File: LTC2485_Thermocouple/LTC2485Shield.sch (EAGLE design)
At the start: 13 parts

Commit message: Added OLED Shield Added LiPo Battery Charger Shield Updated outlines of all shields to match the cutout of the nodemcu board
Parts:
- removed JP1, JP2: (no value), SparkFun:M03LOCK
- added SJ1, SJ2: (no value), SparkFun:SOLDERJUMPER_2WAYT
- D2, D3: device SparkFun:DIODESMB -> SparkFun:DIODESOD
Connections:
- net GND: now also SJ1.1, SJ2.1, U$1.GND$10, U$1.GND$17, U$1.GND$24; no longer JP1.1, JP2.1
- net N$2: now also U$1.D7/GPIO13/RXD2/HSPID/SDA; no longer U$1.D7/GPIO13/RXD2/HSPID
- net N$6: now also SJ1.3, SJ2.3; no longer JP1.3, JP2.3
- net N$7: now also SJ1.2; no longer JP1.2
- net N$8: now also U$1.D6/GPIO12/HSPIQ/SCL; no longer U$1.D6/GPIO12/HSPIQ
- net N$9: now also SJ2.2; no longer JP2.2
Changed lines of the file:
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@@
 <?xml version="1.0" encoding="utf-8"?>
 <!DOCTYPE eagle SYSTEM "eagle.dtd">
-<eagle version="7.3.0">
+<eagle version="7.4.0">
 <drawing>
 <settings>
@@
 <part name="X1" library="con-wago-500" deviceset="W237-102" device=""/>
 <part name="R3" library="SparkFun" deviceset="RESISTOR" device="0402-RES" value="2k"/>
-<part name="D2" library="SparkFun" deviceset="DIODE" device="SMB"/>
-<part name="D3" library="SparkFun" deviceset="DIODE" device="SMB"/>
+<part name="D2" library="SparkFun" deviceset="DIODE" device="SOD"/>
+<part name="D3" library="SparkFun" deviceset="DIODE" device="SOD"/>
 <part name="R4" library="SparkFun" deviceset="RESISTOR" device="0402-RES" value="4.7k"/>
 <part name="P+2" library="SparkFun" deviceset="3.3V" device=""/>
 <part name="GND5" library="SparkFun" deviceset="GND" device=""/>
-<part name="JP1" library="SparkFun" deviceset="M03" device="LOCK"/>
-<part name="JP2" library="SparkFun" deviceset="M03" device="LOCK"/>
 <part name="P+4" library="SparkFun" deviceset="3.3V" device=""/>
+<part name="GND6" library="SparkFun" deviceset="GND" device=""/>
+<part name="SJ1" library="SparkFun" deviceset="SOLDERJUMPER_2WAY" device="T"/>
+<part name="SJ2" library="SparkFun" deviceset="SOLDERJUMPER_2WAY" device="T"/>
 </parts>
 <sheets>
@@
 <instance part="R4" gate="G$1" x="83.82" y="2.54" rot="R90"/>
 <instance part="P+2" gate="G$1" x="83.82" y="10.16"/>
-<instance part="GND5" gate="1" x="127" y="-12.7"/>
-<instance part="JP1" gate="G$1" x="91.44" y="-15.24" rot="R90"/>
-<instance part="JP2" gate="G$1" x="109.22" y="-15.24" rot="R90"/>
+<instance part="GND5" gate="1" x="127" y="-27.94"/>
 <instance part="P+4" gate="G$1" x="167.64" y="50.8"/>
+<instance part="GND6" gate="1" x="73.66" y="20.32"/>
+<instance part="SJ1" gate="G$1" x="91.44" y="-12.7" rot="R270"/>
+<instance part="SJ2" gate="G$1" x="109.22" y="-12.7" rot="R270"/>
 </instances>
 <busses>
@@
 <wire x1="7.62" y1="33.02" x2="-5.08" y2="33.02" width="0.1524" layer="91"/>
 <wire x1="-5.08" y1="33.02" x2="-5.08" y2="20.32" width="0.1524" layer="91"/>
+<pinref part="U$1" gate="G$1" pin="GND$10"/>
+<wire x1="7.62" y1="43.18" x2="-5.08" y2="43.18" width="0.1524" layer="91"/>
+<wire x1="-5.08" y1="43.18" x2="-5.08" y2="33.02" width="0.1524" layer="91"/>
+<junction x="-5.08" y="33.02"/>
 </segment>
 <segment>
@@
 </segment>
 <segment>
-<pinref part="JP1" gate="G$1" pin="1"/>
-<wire x1="93.98" y1="-7.62" x2="93.98" y2="-2.54" width="0.1524" layer="91"/>
 <pinref part="GND5" gate="1" pin="GND"/>
-<wire x1="93.98" y1="-2.54" x2="111.76" y2="-2.54" width="0.1524" layer="91"/>
-<wire x1="111.76" y1="-2.54" x2="127" y2="-2.54" width="0.1524" layer="91"/>
-<wire x1="127" y1="-2.54" x2="127" y2="-10.16" width="0.1524" layer="91"/>
-<pinref part="JP2" gate="G$1" pin="1"/>
-<wire x1="111.76" y1="-7.62" x2="111.76" y2="-2.54" width="0.1524" layer="91"/>
-<junction x="111.76" y="-2.54"/>
+<wire x1="99.06" y1="-20.32" x2="116.84" y2="-20.32" width="0.1524" layer="91"/>
+<wire x1="116.84" y1="-20.32" x2="127" y2="-20.32" width="0.1524" layer="91"/>
+<wire x1="127" y1="-20.32" x2="127" y2="-25.4" width="0.1524" layer="91"/>
+<junction x="116.84" y="-20.32"/>
+<pinref part="SJ1" gate="G$1" pin="1"/>
+<wire x1="96.52" y1="-12.7" x2="99.06" y2="-12.7" width="0.1524" layer="91"/>
+<wire x1="99.06" y1="-12.7" x2="99.06" y2="-20.32" width="0.1524" layer="91"/>
+<pinref part="SJ2" gate="G$1" pin="1"/>
+<wire x1="114.3" y1="-12.7" x2="116.84" y2="-12.7" width="0.1524" layer="91"/>
+<wire x1="116.84" y1="-12.7" x2="116.84" y2="-20.32" width="0.1524" layer="91"/>
+</segment>
+<segment>
+<pinref part="U$1" gate="G$1" pin="GND$17"/>
+<pinref part="GND6" gate="1" pin="GND"/>
+<wire x1="71.12" y1="33.02" x2="73.66" y2="33.02" width="0.1524" layer="91"/>
+<wire x1="73.66" y1="33.02" x2="73.66" y2="22.86" width="0.1524" layer="91"/>
+<pinref part="U$1" gate="G$1" pin="GND$24"/>
+<wire x1="71.12" y1="50.8" x2="73.66" y2="50.8" width="0.1524" layer="91"/>
+<wire x1="73.66" y1="50.8" x2="73.66" y2="33.02" width="0.1524" layer="91"/>
+<junction x="73.66" y="33.02"/>
 </segment>
 </net>
@@
 <net name="N$2" class="0">
 <segment>
-<pinref part="U$1" gate="G$1" pin="D7/GPIO13/RXD2/HSPID"/>
+<pinref part="U$1" gate="G$1" pin="D7/GPIO13/RXD2/HSPID/SDA"/>
 <wire x1="121.92" y1="43.18" x2="104.14" y2="43.18" width="0.1524" layer="91"/>
 <pinref part="U$2" gate="G$2" pin="SDA"/>
@@
 <net name="N$8" class="0">
 <segment>
-<pinref part="U$1" gate="G$1" pin="D6/GPIO12/HSPIQ"/>
+<pinref part="U$1" gate="G$1" pin="D6/GPIO12/HSPIQ/SCL"/>
 <pinref part="U$2" gate="G$2" pin="SCL"/>
 <wire x1="121.92" y1="45.72" x2="96.52" y2="45.72" width="0.1524" layer="91"/>
@@
 <pinref part="R4" gate="G$1" pin="1"/>
 <wire x1="83.82" y1="-2.54" x2="83.82" y2="-5.08" width="0.1524" layer="91"/>
-<pinref part="JP2" gate="G$1" pin="3"/>
-<wire x1="83.82" y1="-5.08" x2="88.9" y2="-5.08" width="0.1524" layer="91"/>
-<wire x1="88.9" y1="-5.08" x2="106.68" y2="-5.08" width="0.1524" layer="91"/>
-<wire x1="106.68" y1="-5.08" x2="106.68" y2="-7.62" width="0.1524" layer="91"/>
-<pinref part="JP1" gate="G$1" pin="3"/>
-<wire x1="88.9" y1="-5.08" x2="88.9" y2="-7.62" width="0.1524" layer="91"/>
-<junction x="88.9" y="-5.08"/>
+<wire x1="83.82" y1="-5.08" x2="101.6" y2="-5.08" width="0.1524" layer="91"/>
+<wire x1="101.6" y1="-5.08" x2="101.6" y2="-12.7" width="0.1524" layer="91"/>
+<junction x="83.82" y="-5.08"/>
+<pinref part="SJ1" gate="G$1" pin="3"/>
+<wire x1="86.36" y1="-12.7" x2="83.82" y2="-12.7" width="0.1524" layer="91"/>
+<wire x1="83.82" y1="-12.7" x2="83.82" y2="-5.08" width="0.1524" layer="91"/>
+<pinref part="SJ2" gate="G$1" pin="3"/>
+<wire x1="104.14" y1="-12.7" x2="101.6" y2="-12.7" width="0.1524" layer="91"/>
 </segment>
 </net>
@@
 <segment>
 <pinref part="U$2" gate="G$2" pin="A1"/>
-<pinref part="JP1" gate="G$1" pin="2"/>
 <wire x1="121.92" y1="38.1" x2="91.44" y2="38.1" width="0.1524" layer="91"/>
 <wire x1="91.44" y1="38.1" x2="91.44" y2="-7.62" width="0.1524" layer="91"/>
+<pinref part="SJ1" gate="G$1" pin="2"/>
 </segment>
 </net>
@@
 <segment>
 <pinref part="U$2" gate="G$2" pin="A0"/>
-<pinref part="JP2" gate="G$1" pin="2"/>
 <wire x1="121.92" y1="35.56" x2="109.22" y2="35.56" width="0.1524" layer="91"/>
 <wire x1="109.22" y1="35.56" x2="109.22" y2="-7.62" width="0.1524" layer="91"/>
-</segment>
-</net>
+<pinref part="SJ2" gate="G$1" pin="2"/>
+</segment>
+</net>

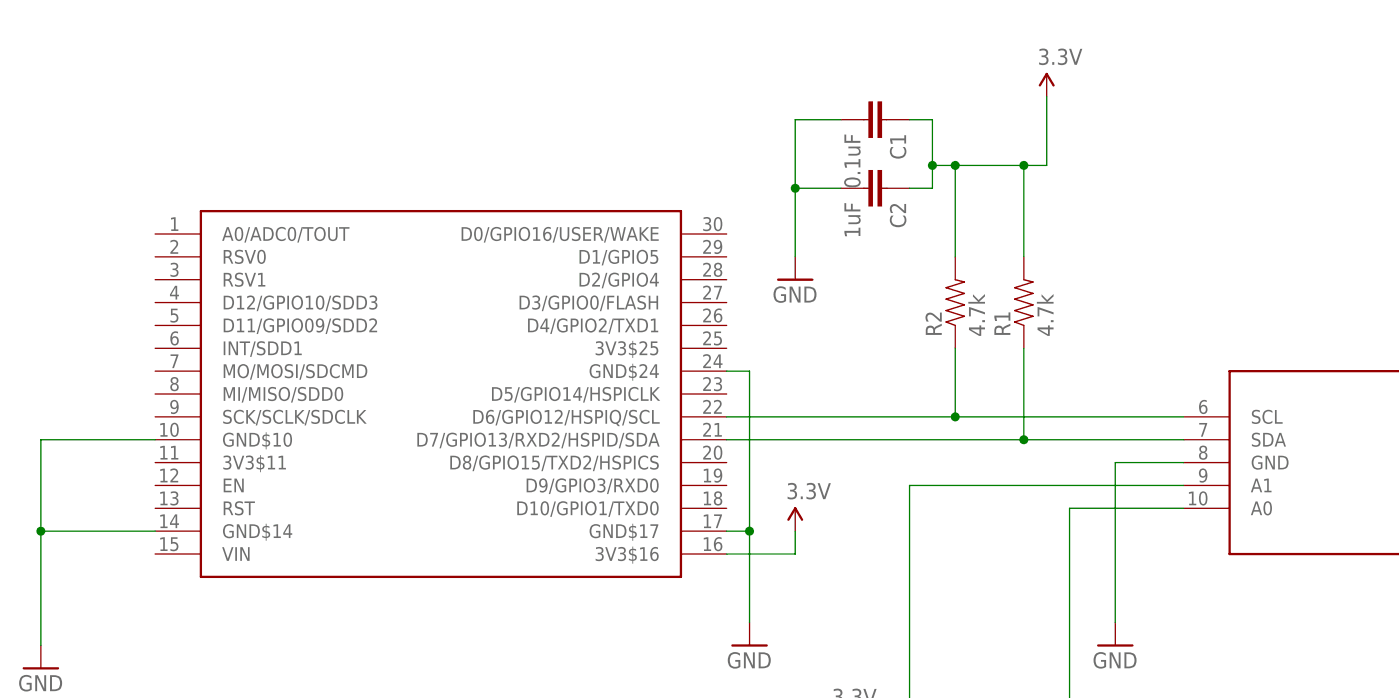
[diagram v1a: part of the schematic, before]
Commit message: Updated the i2c pins to all shields to use d11/d12  as these pins will have dual use with the upcoming wifimcu Added FM24W256  Fram shield Added X95840 Digital potentiometer Shield Added AD5696 DAC Shield
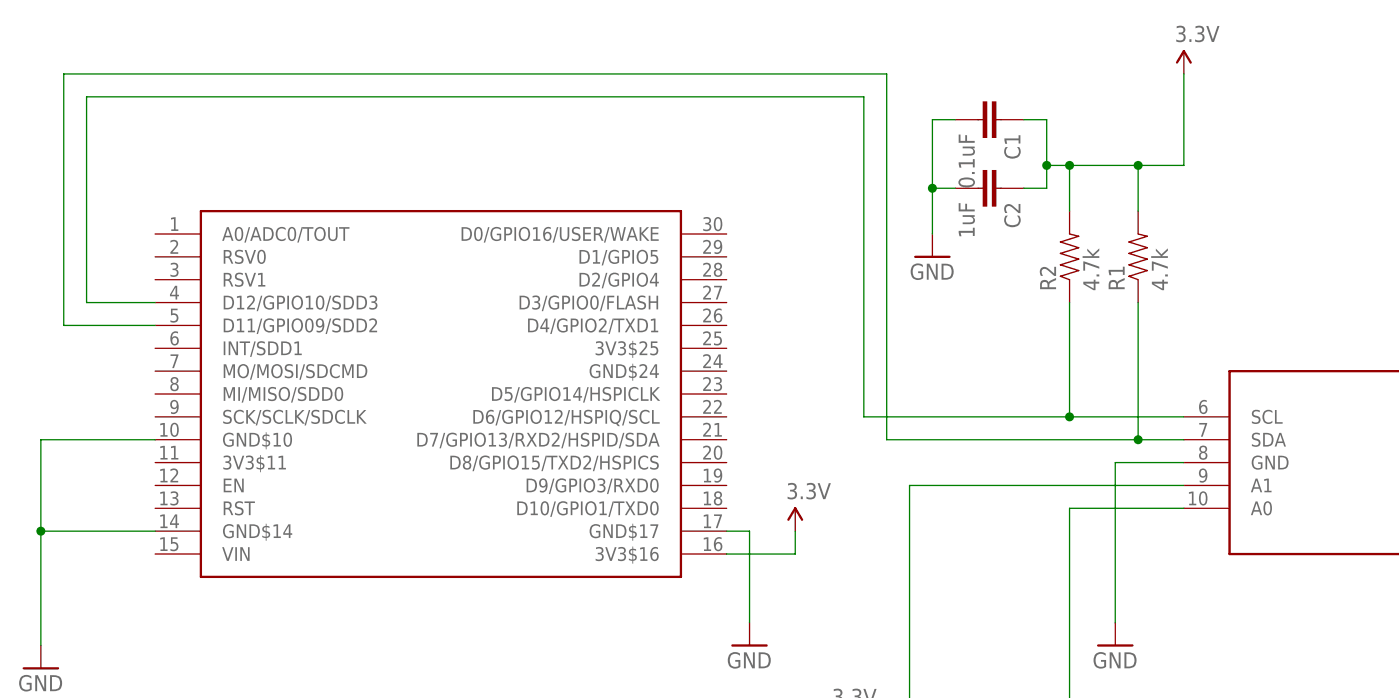
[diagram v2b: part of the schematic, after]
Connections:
- net GND: no longer U$1.GND$24
- net N$2: now also U$1.D11/GPIO09/SDD2; no longer U$1.D7/GPIO13/RXD2/HSPID/SDA
- net N$8: now also U$1.D12/GPIO10/SDD3; no longer U$1.D6/GPIO12/HSPIQ/SCL
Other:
- moved on the sheet: C1, C2, R1, R2
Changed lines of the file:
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@@
 <instance part="U$1" gate="G$1" x="25.4" y="48.26"/>
 <instance part="GND1" gate="1" x="-5.08" y="17.78"/>
-<instance part="GND2" gate="1" x="78.74" y="60.96"/>
+<instance part="GND2" gate="1" x="93.98" y="63.5"/>
 <instance part="P+1" gate="G$1" x="78.74" y="33.02"/>
-<instance part="R1" gate="G$1" x="104.14" y="58.42" rot="R90"/>
-<instance part="R2" gate="G$1" x="96.52" y="58.42" rot="R90"/>
-<instance part="C1" gate="G$1" x="86.36" y="78.74" rot="R270"/>
-<instance part="P+3" gate="G$1" x="106.68" y="81.28"/>
-<instance part="C2" gate="G$1" x="86.36" y="71.12" rot="R270"/>
+<instance part="R1" gate="G$1" x="116.84" y="63.5" rot="R90"/>
+<instance part="R2" gate="G$1" x="109.22" y="63.5" rot="R90"/>
+<instance part="C1" gate="G$1" x="99.06" y="78.74" rot="R270"/>
+<instance part="P+3" gate="G$1" x="121.92" y="83.82"/>
+<instance part="C2" gate="G$1" x="99.06" y="71.12" rot="R270"/>
 <instance part="U$2" gate="G$2" x="144.78" y="53.34" rot="R180"/>
 <instance part="GND3" gate="1" x="114.3" y="20.32"/>
@@
 <pinref part="C1" gate="G$1" pin="2"/>
 <pinref part="GND2" gate="1" pin="GND"/>
-<wire x1="83.82" y1="78.74" x2="78.74" y2="78.74" width="0.1524" layer="91"/>
-<wire x1="78.74" y1="78.74" x2="78.74" y2="71.12" width="0.1524" layer="91"/>
+<wire x1="96.52" y1="78.74" x2="93.98" y2="78.74" width="0.1524" layer="91"/>
+<wire x1="93.98" y1="78.74" x2="93.98" y2="71.12" width="0.1524" layer="91"/>
 <pinref part="C2" gate="G$1" pin="2"/>
-<wire x1="78.74" y1="71.12" x2="78.74" y2="63.5" width="0.1524" layer="91"/>
-<wire x1="83.82" y1="71.12" x2="78.74" y2="71.12" width="0.1524" layer="91"/>
-<junction x="78.74" y="71.12"/>
+<wire x1="93.98" y1="71.12" x2="93.98" y2="66.04" width="0.1524" layer="91"/>
+<wire x1="96.52" y1="71.12" x2="93.98" y2="71.12" width="0.1524" layer="91"/>
+<junction x="93.98" y="71.12"/>
 </segment>
 <segment>
@@
 <wire x1="71.12" y1="33.02" x2="73.66" y2="33.02" width="0.1524" layer="91"/>
 <wire x1="73.66" y1="33.02" x2="73.66" y2="22.86" width="0.1524" layer="91"/>
-<pinref part="U$1" gate="G$1" pin="GND$24"/>
-<wire x1="71.12" y1="50.8" x2="73.66" y2="50.8" width="0.1524" layer="91"/>
-<wire x1="73.66" y1="50.8" x2="73.66" y2="33.02" width="0.1524" layer="91"/>
-<junction x="73.66" y="33.02"/>
 </segment>
 </net>
@@
 <segment>
 <pinref part="R2" gate="G$1" pin="2"/>
-<wire x1="96.52" y1="63.5" x2="96.52" y2="73.66" width="0.1524" layer="91"/>
+<wire x1="109.22" y1="68.58" x2="109.22" y2="73.66" width="0.1524" layer="91"/>
 <pinref part="P+3" gate="G$1" pin="3.3V"/>
-<wire x1="96.52" y1="73.66" x2="104.14" y2="73.66" width="0.1524" layer="91"/>
-<wire x1="104.14" y1="73.66" x2="106.68" y2="73.66" width="0.1524" layer="91"/>
-<wire x1="106.68" y1="73.66" x2="106.68" y2="81.28" width="0.1524" layer="91"/>
+<wire x1="109.22" y1="73.66" x2="116.84" y2="73.66" width="0.1524" layer="91"/>
+<wire x1="116.84" y1="73.66" x2="121.92" y2="73.66" width="0.1524" layer="91"/>
+<wire x1="121.92" y1="73.66" x2="121.92" y2="83.82" width="0.1524" layer="91"/>
 <pinref part="R1" gate="G$1" pin="2"/>
-<wire x1="104.14" y1="63.5" x2="104.14" y2="73.66" width="0.1524" layer="91"/>
-<junction x="104.14" y="73.66"/>
-<wire x1="96.52" y1="73.66" x2="93.98" y2="73.66" width="0.1524" layer="91"/>
-<wire x1="93.98" y1="73.66" x2="93.98" y2="78.74" width="0.1524" layer="91"/>
-<junction x="96.52" y="73.66"/>
+<wire x1="116.84" y1="68.58" x2="116.84" y2="73.66" width="0.1524" layer="91"/>
+<junction x="116.84" y="73.66"/>
+<wire x1="109.22" y1="73.66" x2="106.68" y2="73.66" width="0.1524" layer="91"/>
+<wire x1="106.68" y1="73.66" x2="106.68" y2="78.74" width="0.1524" layer="91"/>
+<junction x="109.22" y="73.66"/>
 <pinref part="C1" gate="G$1" pin="1"/>
-<wire x1="93.98" y1="78.74" x2="91.44" y2="78.74" width="0.1524" layer="91"/>
-<wire x1="93.98" y1="73.66" x2="93.98" y2="71.12" width="0.1524" layer="91"/>
-<junction x="93.98" y="73.66"/>
+<wire x1="106.68" y1="78.74" x2="104.14" y2="78.74" width="0.1524" layer="91"/>
+<wire x1="106.68" y1="73.66" x2="106.68" y2="71.12" width="0.1524" layer="91"/>
+<junction x="106.68" y="73.66"/>
 <pinref part="C2" gate="G$1" pin="1"/>
-<wire x1="93.98" y1="71.12" x2="91.44" y2="71.12" width="0.1524" layer="91"/>
+<wire x1="106.68" y1="71.12" x2="104.14" y2="71.12" width="0.1524" layer="91"/>
 </segment>
 <segment>
@@
 <net name="N$2" class="0">
 <segment>
-<pinref part="U$1" gate="G$1" pin="D7/GPIO13/RXD2/HSPID/SDA"/>
-<wire x1="121.92" y1="43.18" x2="104.14" y2="43.18" width="0.1524" layer="91"/>
+<wire x1="121.92" y1="43.18" x2="116.84" y2="43.18" width="0.1524" layer="91"/>
 <pinref part="U$2" gate="G$2" pin="SDA"/>
 <pinref part="R1" gate="G$1" pin="1"/>
-<wire x1="104.14" y1="43.18" x2="71.12" y2="43.18" width="0.1524" layer="91"/>
-<wire x1="104.14" y1="53.34" x2="104.14" y2="43.18" width="0.1524" layer="91"/>
-<junction x="104.14" y="43.18"/>
+<wire x1="116.84" y1="43.18" x2="88.9" y2="43.18" width="0.1524" layer="91"/>
+<wire x1="116.84" y1="58.42" x2="116.84" y2="43.18" width="0.1524" layer="91"/>
+<junction x="116.84" y="43.18"/>
+<pinref part="U$1" gate="G$1" pin="D11/GPIO09/SDD2"/>
+<wire x1="7.62" y1="55.88" x2="-2.54" y2="55.88" width="0.1524" layer="91"/>
+<wire x1="-2.54" y1="55.88" x2="-2.54" y2="83.82" width="0.1524" layer="91"/>
+<wire x1="-2.54" y1="83.82" x2="88.9" y2="83.82" width="0.1524" layer="91"/>
+<wire x1="88.9" y1="83.82" x2="88.9" y2="43.18" width="0.1524" layer="91"/>
 </segment>
 </net>
 <net name="N$8" class="0">
 <segment>
-<pinref part="U$1" gate="G$1" pin="D6/GPIO12/HSPIQ/SCL"/>
 <pinref part="U$2" gate="G$2" pin="SCL"/>
-<wire x1="121.92" y1="45.72" x2="96.52" y2="45.72" width="0.1524" layer="91"/>
+<wire x1="121.92" y1="45.72" x2="109.22" y2="45.72" width="0.1524" layer="91"/>
 <pinref part="R2" gate="G$1" pin="1"/>
-<wire x1="96.52" y1="45.72" x2="71.12" y2="45.72" width="0.1524" layer="91"/>
-<wire x1="96.52" y1="53.34" x2="96.52" y2="45.72" width="0.1524" layer="91"/>
-<junction x="96.52" y="45.72"/>
+<wire x1="109.22" y1="45.72" x2="86.36" y2="45.72" width="0.1524" layer="91"/>
+<wire x1="109.22" y1="58.42" x2="109.22" y2="45.72" width="0.1524" layer="91"/>
+<junction x="109.22" y="45.72"/>
+<wire x1="86.36" y1="45.72" x2="86.36" y2="81.28" width="0.1524" layer="91"/>
+<wire x1="86.36" y1="81.28" x2="0" y2="81.28" width="0.1524" layer="91"/>
+<wire x1="0" y1="81.28" x2="0" y2="58.42" width="0.1524" layer="91"/>
+<pinref part="U$1" gate="G$1" pin="D12/GPIO10/SDD3"/>
+<wire x1="0" y1="58.42" x2="7.62" y2="58.42" width="0.1524" layer="91"/>
 </segment>
 </net>
